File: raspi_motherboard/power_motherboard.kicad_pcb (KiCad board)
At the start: 4 copper layers, 65 x 57.1 mm, 62 parts, among them J1 GPIO, J2 Conn_02x04_Top_Bottom, U1 LTC4412xS6, U2 MCP2515-xST, U3 SN65HVD230, U4 LMZM33606RLXR, Y1 Crystal, x2 10µ, x2.2 47µ, x2.3 47µ

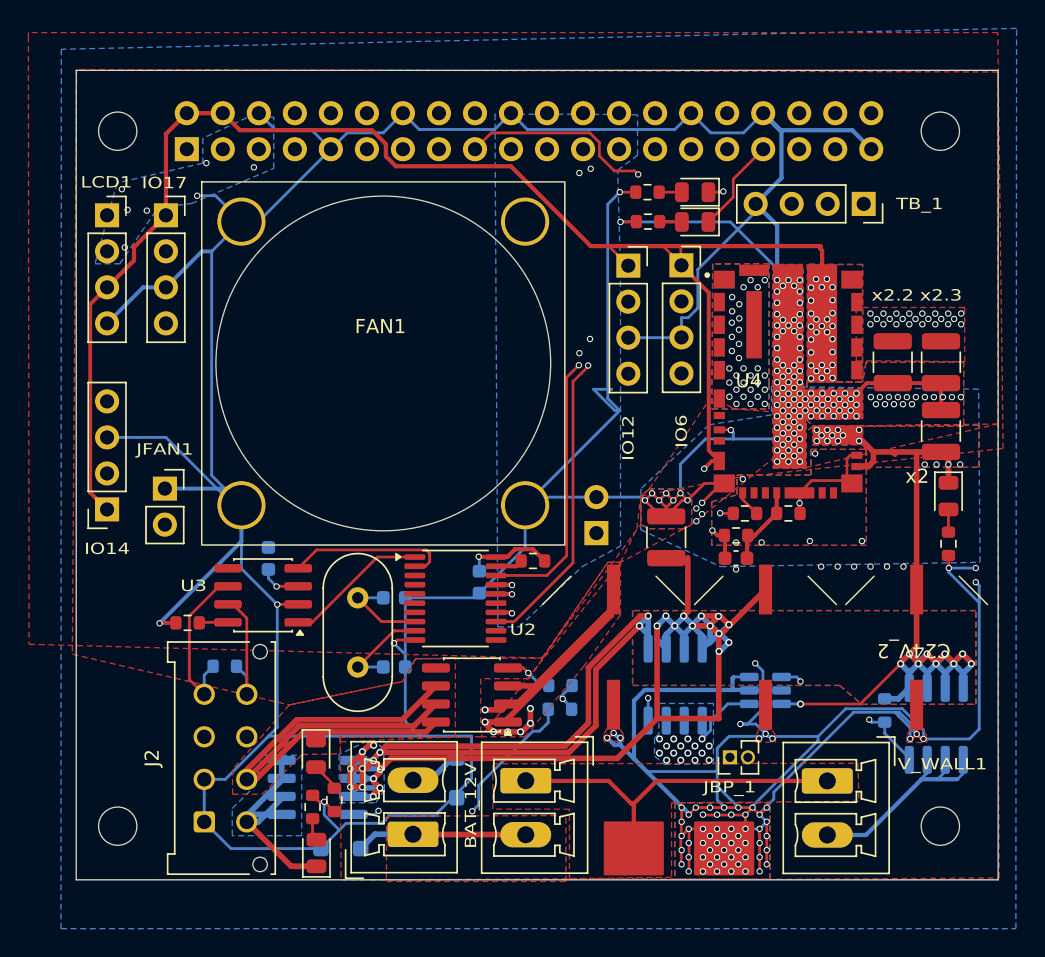
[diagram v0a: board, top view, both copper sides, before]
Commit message: Changing connectors
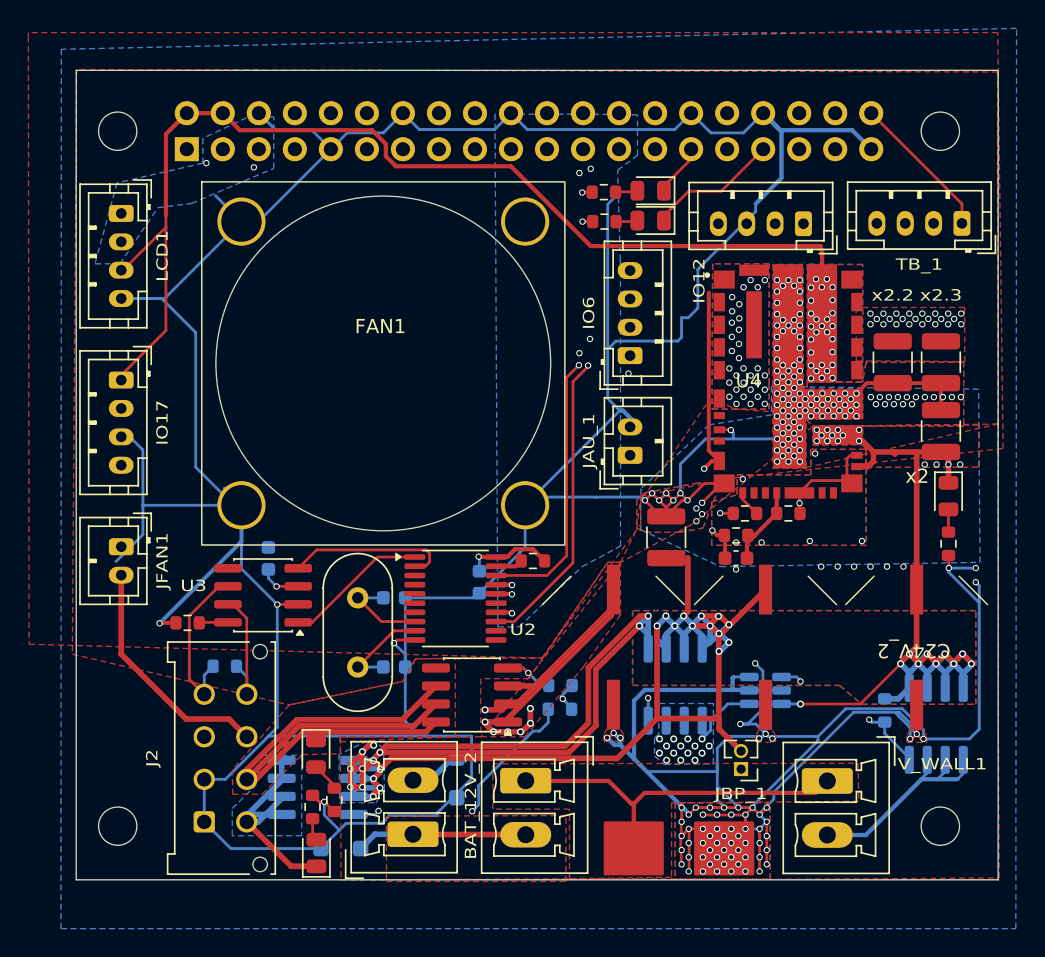
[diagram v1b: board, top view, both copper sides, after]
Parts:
- removed IO14: Conn_01x04_Socket, Connector_PinSocket_2.54mm:PinSocket_1x04_P2.54mm_Vertical
- IO12, IO17, IO6, LCD1, TB_1: footprint Connector_PinSocket_2.54mm:PinSocket_1x04_P2.54mm_Vertical -> Connector_JST:JST_PH_B4B-PH-K_1x04_P2.00mm_Vertical
- JAU_1: footprint Connector_PinSocket_2.54mm:PinSocket_1x02_P2.54mm_Vertical -> Connector_JST:JST_PH_B2B-PH-K_1x02_P2.00mm_Vertical; moved to F.Cu
- JFAN1: footprint Connector_PinSocket_2.54mm:PinSocket_1x02_P2.54mm_Vertical -> Connector_JST:JST_PH_B2B-PH-K_1x02_P2.00mm_Vertical
- moved IO12 12.7 mm to (151.8, 54.0), turned to 180 degrees
- moved IO17 12.0 mm to (103.8, 65.0), turned to -90 degrees
- moved IO6 7.32 mm to (139.6, 63.3), turned to 90 degrees
- moved TB_1 7.06 mm to (163.0, 54.0), turned to 180 degrees
- moved JAU_1 5.98 mm to (139.6, 70.3), turned to 90 degrees
- moved JFAN1 5.12 mm to (103.8, 76.8), turned to -90 degrees
- moved LED_R_1 3.14 mm to (141.1, 53.8)
- moved LED_R_2 3.14 mm to (141.1, 51.7)
- moved R_LED_R_1 3.07 mm to (137.8, 53.9)
- moved R_LED_R_2 3.07 mm to (137.8, 51.8)
- moved JBP_1 1.14 mm to (147.4, 92.5), turned to 180 degrees
- moved LCD1 1.01 mm to (103.8, 53.3), turned to -90 degrees
- renumbered BAT_12V to BAT_12V_1, BAT_12V to BAT_12V_2
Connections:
- LED_R_2 pad 1: /GPIO26 -> /GPIO5
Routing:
- net R_IO14: track 31.2 -> 0.00 mm
- net 24V_BAT: track 21.5 -> 49.4 mm, vias 16 -> 15
- net GND: track 539.5 -> 520.1 mm, vias 213 -> 208
- net 3_3V: track 133.4 -> 115.9 mm
- net 5V: track 110.5 -> 96.0 mm
- net /GPIO26: track 11.0 -> 0.00 mm, vias 1 -> 0
- net R_IO17: track 17.2 -> 26.4 mm
- net AU: track 15.4 -> 22.4 mm
- net R_IO12: track 16.2 -> 9.20 mm
- net R_IO6: track 12.1 -> 16.4 mm
- net /GPIO5: track 0.00 -> 3.96 mm
- net R_IO16: track 7.98 -> 11.8 mm
- net R_IO20: track 7.77 -> 11.6 mm
- net 12V: track 101.0 -> 97.7 mm
- net 24V: track 226.3 -> 229.3 mm
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
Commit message: Production version
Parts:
- JBP_1: footprint Connector_PinHeader_1.27mm:PinHeader_1x02_P1.27mm_Vertical -> Connector_PinSocket_2.00mm:PinSocket_1x02_P2.00mm_Vertical
- moved JBP_1 2.06 mm to (145.7, 91.4), turned to 90 degrees
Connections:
- net SDL renamed SCL
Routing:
- net GND: track 520.1 -> 519.5 mm
- net 24V_BAT: vias 15 -> 13
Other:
- outline, holes or cut-outs redrawn
